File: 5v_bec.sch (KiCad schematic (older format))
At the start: 9 parts

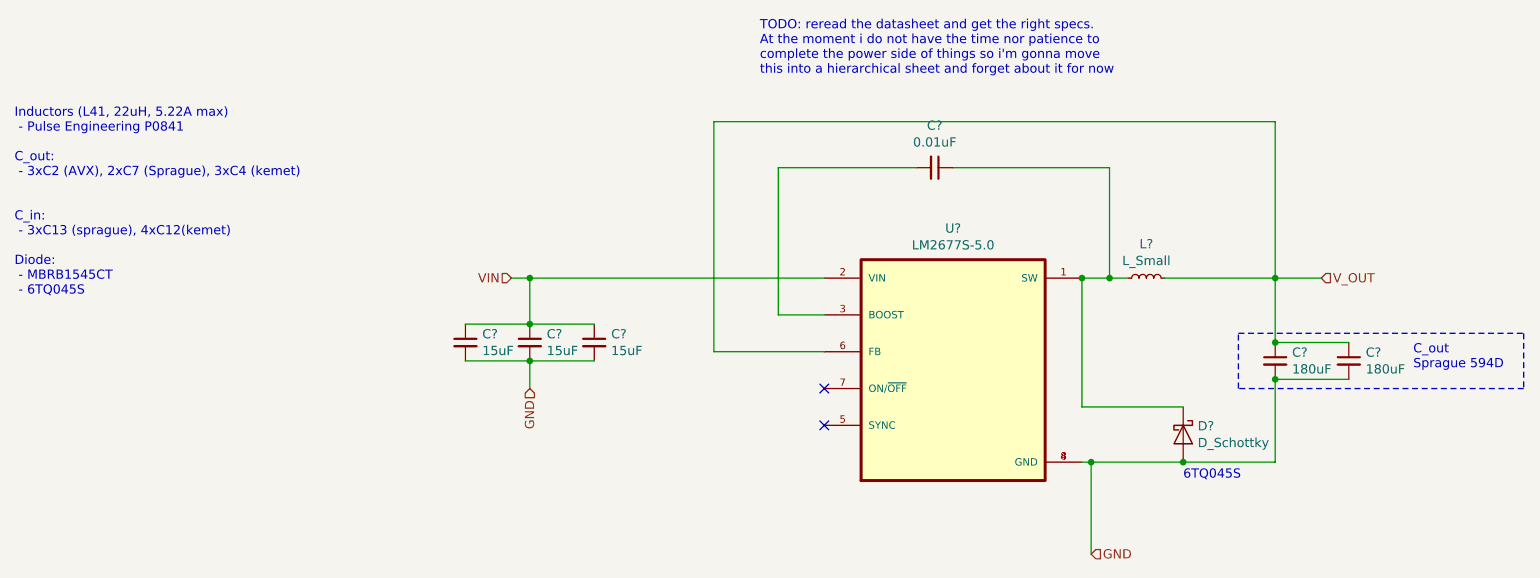
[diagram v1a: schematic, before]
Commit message: update reference ids, assign value to c8
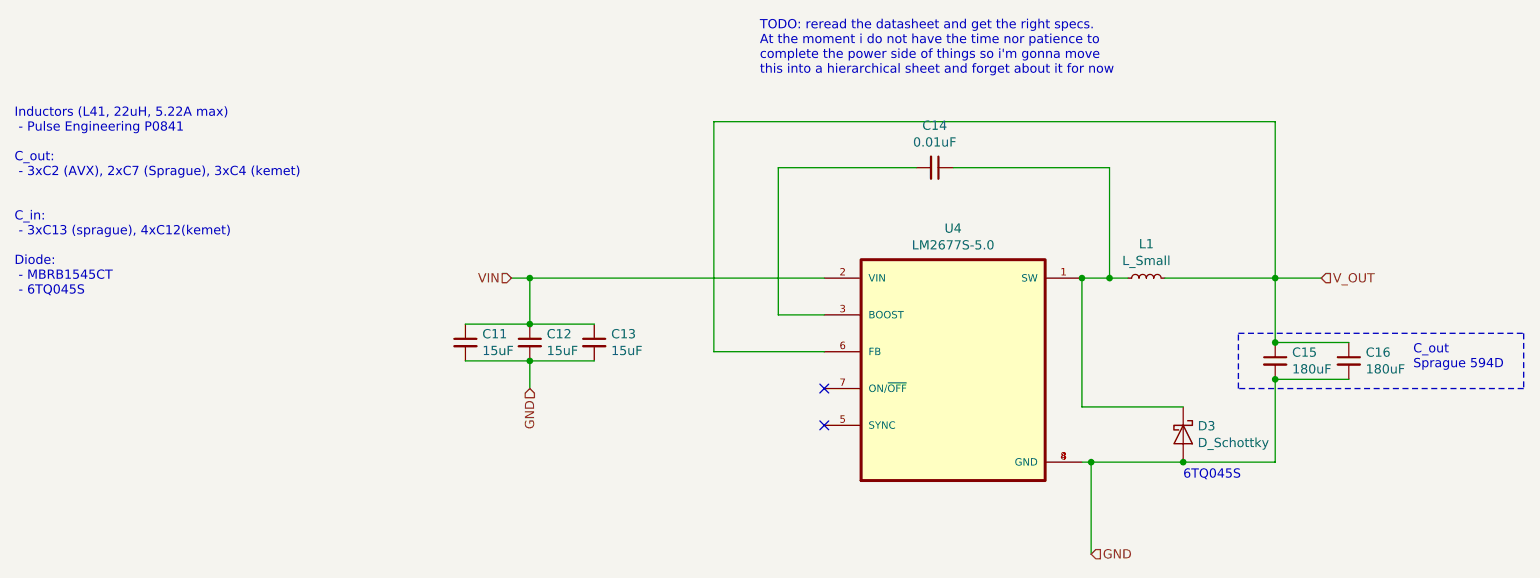
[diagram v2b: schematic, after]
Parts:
- gave numbers to parts that had none: 9
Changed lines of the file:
@@
 $Descr A4 11693 8268
 encoding utf-8
-Sheet 7 8
+Sheet 4 8
 Title ""
 Date ""
@@
 $EndDescr
 $Comp
-L LM2677S-5.0:LM2677S-5.0 U?
+L LM2677S-5.0:LM2677S-5.0 U4
 U 1 1 6175201D
 P 6000 4250
-AR Path="/6175047F/6175201D" Ref="U?"  Part="1"
+AR Path="/6175047F/6175201D" Ref="U4"  Part="1"
 AR Path="/617748F9/6175201D" Ref="U?"  Part="1"
 AR Path="/619B79F1/6175201D" Ref="U?"  Part="1"
-AR Path="/619C4F1E/6175201D" Ref="U?"  Part="1"
+AR Path="/619C4F1E/6175201D" Ref="U7"  Part="1"
 AR Path="/619C86ED/6175201D" Ref="U?"  Part="1"
-F 0 "U?" H 6000 5020 50  0000 C CNN
+F 0 "U4" H 6000 5020 50  0000 C CNN
 F 1 "LM2677S-5.0" H 6000 4929 50  0000 C CNN
 F 2 "TO127P1435X464-8N" H 6000 4250 50  0001 L BNN
@@
 	6750 4750 6700 4750
 $Comp
-L Device:D_Schottky D?
+L Device:D_Schottky D3
 U 1 1 617603E2
 P 7250 4600
-AR Path="/6175047F/617603E2" Ref="D?"  Part="1"
+AR Path="/6175047F/617603E2" Ref="D3"  Part="1"
 AR Path="/617748F9/617603E2" Ref="D?"  Part="1"
 AR Path="/619B79F1/617603E2" Ref="D?"  Part="1"
-AR Path="/619C4F1E/617603E2" Ref="D?"  Part="1"
+AR Path="/619C4F1E/617603E2" Ref="D6"  Part="1"
 AR Path="/619C86ED/617603E2" Ref="D?"  Part="1"
-F 0 "D?" V 7204 4679 50  0000 L CNN
+F 0 "D3" V 7204 4679 50  0000 L CNN
 F 1 "D_Schottky" V 7295 4679 50  0000 L CNN
 F 2 "" H 7250 4600 50  0001 C CNN
@@
 	6750 4750 7250 4750
 $Comp
-L Device:L_Small L?
+L Device:L_Small L1
 U 1 1 61768ED3
 P 7050 3750
-AR Path="/6175047F/61768ED3" Ref="L?"  Part="1"
+AR Path="/6175047F/61768ED3" Ref="L1"  Part="1"
 AR Path="/617748F9/61768ED3" Ref="L?"  Part="1"
 AR Path="/619B79F1/61768ED3" Ref="L?"  Part="1"
-AR Path="/619C4F1E/61768ED3" Ref="L?"  Part="1"
+AR Path="/619C4F1E/61768ED3" Ref="L2"  Part="1"
 AR Path="/619C86ED/61768ED3" Ref="L?"  Part="1"
-F 0 "L?" V 7235 3750 50  0000 C CNN
+F 0 "L1" V 7235 3750 50  0000 C CNN
 F 1 "L_Small" V 7144 3750 50  0000 C CNN
 F 2 "" H 7050 3750 50  0001 C CNN
@@
 	6850 3750 6950 3750
 $Comp
-L Device:C_Small C?
+L Device:C_Small C14
 U 1 1 6176CADF
 P 5900 3150
-AR Path="/6175047F/6176CADF" Ref="C?"  Part="1"
+AR Path="/6175047F/6176CADF" Ref="C14"  Part="1"
 AR Path="/617748F9/6176CADF" Ref="C?"  Part="1"
 AR Path="/619B79F1/6176CADF" Ref="C?"  Part="1"
-AR Path="/619C4F1E/6176CADF" Ref="C?"  Part="1"
+AR Path="/619C4F1E/6176CADF" Ref="C25"  Part="1"
 AR Path="/619C86ED/6176CADF" Ref="C?"  Part="1"
-F 0 "C?" V 5671 3150 50  0000 C CNN
+F 0 "C14" V 5671 3150 50  0000 C CNN
 F 1 "0.01uF" V 5762 3150 50  0000 C CNN
 F 2 "" H 5900 3150 50  0001 C CNN
@@
 Inductors (L41, 22uH, 5.22A max)\n - Pulse Engineering P0841\n\nC_out:\n - 3xC2 (AVX), 2xC7 (Sprague), 3xC4 (kemet)\n\n\nC_in:\n - 3xC13 (sprague), 4xC12(kemet)\n\nDiode: \n - MBRB1545CT\n - 6TQ045S
 $Comp
-L Device:C_Small C?
+L Device:C_Small C15
 U 1 1 61A51E59
 P 7750 4200
-AR Path="/6175047F/61A51E59" Ref="C?"  Part="1"
-AR Path="/619C4F1E/61A51E59" Ref="C?"  Part="1"
-F 0 "C?" H 7842 4246 50  0000 L CNN
+AR Path="/6175047F/61A51E59" Ref="C15"  Part="1"
+AR Path="/619C4F1E/61A51E59" Ref="C26"  Part="1"
+F 0 "C15" H 7842 4246 50  0000 L CNN
 F 1 "180uF" H 7842 4155 50  0000 L CNN
 F 2 "" H 7750 4200 50  0001 C CNN
@@
 $EndComp
 $Comp
-L Device:C_Small C?
+L Device:C_Small C16
 U 1 1 61A52F3A
 P 8150 4200
-AR Path="/6175047F/61A52F3A" Ref="C?"  Part="1"
-AR Path="/619C4F1E/61A52F3A" Ref="C?"  Part="1"
-F 0 "C?" H 8242 4246 50  0000 L CNN
+AR Path="/6175047F/61A52F3A" Ref="C16"  Part="1"
+AR Path="/619C4F1E/61A52F3A" Ref="C27"  Part="1"
+F 0 "C16" H 8242 4246 50  0000 L CNN
 F 1 "180uF" H 8242 4155 50  0000 L CNN
 F 2 "" H 8150 4200 50  0001 C CNN
@@
 	3600 3750 3700 3750
 $Comp
-L Device:C_Small C?
+L Device:C_Small C11
 U 1 1 61A5F9C8
 P 3350 4100
-AR Path="/6175047F/61A5F9C8" Ref="C?"  Part="1"
-AR Path="/619C4F1E/61A5F9C8" Ref="C?"  Part="1"
-F 0 "C?" H 3442 4146 50  0000 L CNN
+AR Path="/6175047F/61A5F9C8" Ref="C11"  Part="1"
+AR Path="/619C4F1E/61A5F9C8" Ref="C22"  Part="1"
+F 0 "C11" H 3442 4146 50  0000 L CNN
 F 1 "15uF" H 3442 4055 50  0000 L CNN
 F 2 "" H 3350 4100 50  0001 C CNN
@@
 $EndComp
 $Comp
-L Device:C_Small C?
+L Device:C_Small C12
 U 1 1 61A60CAD
 P 3700 4100
-AR Path="/6175047F/61A60CAD" Ref="C?"  Part="1"
-AR Path="/619C4F1E/61A60CAD" Ref="C?"  Part="1"
-F 0 "C?" H 3792 4146 50  0000 L CNN
+AR Path="/6175047F/61A60CAD" Ref="C12"  Part="1"
+AR Path="/619C4F1E/61A60CAD" Ref="C23"  Part="1"
+F 0 "C12" H 3792 4146 50  0000 L CNN
 F 1 "15uF" H 3792 4055 50  0000 L CNN
 F 2 "" H 3700 4100 50  0001 C CNN
@@
 $EndComp
 $Comp
-L Device:C_Small C?
+L Device:C_Small C13
 U 1 1 61A62459
 P 4050 4100
-AR Path="/6175047F/61A62459" Ref="C?"  Part="1"
-AR Path="/619C4F1E/61A62459" Ref="C?"  Part="1"
-F 0 "C?" H 4142 4146 50  0000 L CNN
+AR Path="/6175047F/61A62459" Ref="C13"  Part="1"
+AR Path="/619C4F1E/61A62459" Ref="C24"  Part="1"
+F 0 "C13" H 4142 4146 50  0000 L CNN
 F 1 "15uF" H 4142 4055 50  0000 L CNN
 F 2 "" H 4050 4100 50  0001 C CNN

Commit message: no longer a hat lol
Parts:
- C11, C12, C13: footprint (none) -> Capacitor_Tantalum_SMD:CP_EIA-7260-15_AVX-R_Pad2.68x6.30mm_HandSolder
- C14: footprint (none) -> Capacitor_SMD:C_0805_2012Metric_Pad1.15x1.40mm_HandSolder
- C15, C16: footprint (none) -> Capacitor_Tantalum_SMD:CP_EIA-7260-38_AVX-R_Pad2.68x6.30mm_HandSolder
- D3: footprint (none) -> TO254P1521X483-4N:TO254P1521X483-4N
- L1: value L_Small -> 22uH; footprint (none) -> Inductor_SMD:L_10.4x10.4_H4.8
- U4: footprint TO127P1435X464-8N -> LM2677S-5:TO127P1435X464-8N
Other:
- note added: "C_in\nSprague 594D"
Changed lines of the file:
@@
 $Descr A4 11693 8268
 encoding utf-8
-Sheet 4 8
+Sheet 7 8
 Title ""
 Date ""
@@
 AR Path="/619C4F1E/6175201D" Ref="U7"  Part="1"
 AR Path="/619C86ED/6175201D" Ref="U?"  Part="1"
-F 0 "U4" H 6000 5020 50  0000 C CNN
+F 0 "U7" H 6000 5020 50  0000 C CNN
 F 1 "LM2677S-5.0" H 6000 4929 50  0000 C CNN
-F 2 "TO127P1435X464-8N" H 6000 4250 50  0001 L BNN
+F 2 "LM2677S-5:TO127P1435X464-8N" H 6000 4250 50  0001 L BNN
 F 3 "" H 6000 4250 50  0001 L BNN
 	1    6000 4250
@@
 AR Path="/619C4F1E/617603E2" Ref="D6"  Part="1"
 AR Path="/619C86ED/617603E2" Ref="D?"  Part="1"
-F 0 "D3" V 7204 4679 50  0000 L CNN
+F 0 "D6" V 7204 4679 50  0000 L CNN
 F 1 "D_Schottky" V 7295 4679 50  0000 L CNN
-F 2 "" H 7250 4600 50  0001 C CNN
+F 2 "TO254P1521X483-4N:TO254P1521X483-4N" H 7250 4600 50  0001 C CNN
 F 3 "~" H 7250 4600 50  0001 C CNN
 	1    7250 4600
@@
 AR Path="/619C4F1E/61768ED3" Ref="L2"  Part="1"
 AR Path="/619C86ED/61768ED3" Ref="L?"  Part="1"
-F 0 "L1" V 7235 3750 50  0000 C CNN
-F 1 "L_Small" V 7144 3750 50  0000 C CNN
-F 2 "" H 7050 3750 50  0001 C CNN
+F 0 "L2" V 7235 3750 50  0000 C CNN
+F 1 "22uH" V 7144 3750 50  0000 C CNN
+F 2 "Inductor_SMD:L_10.4x10.4_H4.8" H 7050 3750 50  0001 C CNN
 F 3 "~" H 7050 3750 50  0001 C CNN
 	1    7050 3750
@@
 AR Path="/619C4F1E/6176CADF" Ref="C25"  Part="1"
 AR Path="/619C86ED/6176CADF" Ref="C?"  Part="1"
-F 0 "C14" V 5671 3150 50  0000 C CNN
+F 0 "C25" V 5671 3150 50  0000 C CNN
 F 1 "0.01uF" V 5762 3150 50  0000 C CNN
-F 2 "" H 5900 3150 50  0001 C CNN
+F 2 "Capacitor_SMD:C_0805_2012Metric_Pad1.15x1.40mm_HandSolder" H 5900 3150 50  0001 C CNN
 F 3 "~" H 5900 3150 50  0001 C CNN
 	1    5900 3150
@@
 AR Path="/6175047F/61A51E59" Ref="C15"  Part="1"
 AR Path="/619C4F1E/61A51E59" Ref="C26"  Part="1"
-F 0 "C15" H 7842 4246 50  0000 L CNN
+F 0 "C26" H 7842 4246 50  0000 L CNN
 F 1 "180uF" H 7842 4155 50  0000 L CNN
-F 2 "" H 7750 4200 50  0001 C CNN
+F 2 "Capacitor_Tantalum_SMD:CP_EIA-7260-38_AVX-R_Pad2.68x6.30mm_HandSolder" H 7750 4200 50  0001 C CNN
 F 3 "~" H 7750 4200 50  0001 C CNN
 	1    7750 4200
@@
 AR Path="/6175047F/61A52F3A" Ref="C16"  Part="1"
 AR Path="/619C4F1E/61A52F3A" Ref="C27"  Part="1"
-F 0 "C16" H 8242 4246 50  0000 L CNN
+F 0 "C27" H 8242 4246 50  0000 L CNN
 F 1 "180uF" H 8242 4155 50  0000 L CNN
-F 2 "" H 8150 4200 50  0001 C CNN
+F 2 "Capacitor_Tantalum_SMD:CP_EIA-7260-38_AVX-R_Pad2.68x6.30mm_HandSolder" H 8150 4200 50  0001 C CNN
 F 3 "~" H 8150 4200 50  0001 C CNN
 	1    8150 4200
@@
 AR Path="/6175047F/61A5F9C8" Ref="C11"  Part="1"
 AR Path="/619C4F1E/61A5F9C8" Ref="C22"  Part="1"
-F 0 "C11" H 3442 4146 50  0000 L CNN
+F 0 "C22" H 3442 4146 50  0000 L CNN
 F 1 "15uF" H 3442 4055 50  0000 L CNN
-F 2 "" H 3350 4100 50  0001 C CNN
+F 2 "Capacitor_Tantalum_SMD:CP_EIA-7260-15_AVX-R_Pad2.68x6.30mm_HandSolder" H 3350 4100 50  0001 C CNN
 F 3 "~" H 3350 4100 50  0001 C CNN
 	1    3350 4100
@@
 AR Path="/6175047F/61A60CAD" Ref="C12"  Part="1"
 AR Path="/619C4F1E/61A60CAD" Ref="C23"  Part="1"
-F 0 "C12" H 3792 4146 50  0000 L CNN
+F 0 "C23" H 3792 4146 50  0000 L CNN
 F 1 "15uF" H 3792 4055 50  0000 L CNN
-F 2 "" H 3700 4100 50  0001 C CNN
+F 2 "Capacitor_Tantalum_SMD:CP_EIA-7260-15_AVX-R_Pad2.68x6.30mm_HandSolder" H 3700 4100 50  0001 C CNN
 F 3 "~" H 3700 4100 50  0001 C CNN
 	1    3700 4100
@@
 AR Path="/6175047F/61A62459" Ref="C13"  Part="1"
 AR Path="/619C4F1E/61A62459" Ref="C24"  Part="1"
-F 0 "C13" H 4142 4146 50  0000 L CNN
+F 0 "C24" H 4142 4146 50  0000 L CNN
 F 1 "15uF" H 4142 4055 50  0000 L CNN
-F 2 "" H 4050 4100 50  0001 C CNN
+F 2 "Capacitor_Tantalum_SMD:CP_EIA-7260-15_AVX-R_Pad2.68x6.30mm_HandSolder" H 4050 4100 50  0001 C CNN
 F 3 "~" H 4050 4100 50  0001 C CNN
 	1    4050 4100
@@
 Text Notes 7250 4850 0    50   ~ 0
 6TQ045S
+Wire Notes Line
+	4400 4300 2700 4300
+Wire Notes Line
+	2700 4300 2700 3900
+Wire Notes Line
+	2700 3900 4400 3900
+Wire Notes Line
+	4400 3900 4400 4300
+Text Notes 2750 4250 0    50   ~ 0
+C_in\nSprague 594D
 $EndSCHEMATC

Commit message: power supply overhaul
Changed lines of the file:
@@
 $Descr A4 11693 8268
 encoding utf-8
-Sheet 7 8
+Sheet 7 10
 Title ""
 Date ""
@@
 AR Path="/619C4F1E/6175201D" Ref="U7"  Part="1"
 AR Path="/619C86ED/6175201D" Ref="U?"  Part="1"
-F 0 "U7" H 6000 5020 50  0000 C CNN
+F 0 "U4" H 6000 5020 50  0000 C CNN
 F 1 "LM2677S-5.0" H 6000 4929 50  0000 C CNN
 F 2 "LM2677S-5:TO127P1435X464-8N" H 6000 4250 50  0001 L BNN
@@
 AR Path="/619C4F1E/617603E2" Ref="D6"  Part="1"
 AR Path="/619C86ED/617603E2" Ref="D?"  Part="1"
-F 0 "D6" V 7204 4679 50  0000 L CNN
+F 0 "D3" V 7204 4679 50  0000 L CNN
 F 1 "D_Schottky" V 7295 4679 50  0000 L CNN
 F 2 "TO254P1521X483-4N:TO254P1521X483-4N" H 7250 4600 50  0001 C CNN
@@
 AR Path="/619C4F1E/61768ED3" Ref="L2"  Part="1"
 AR Path="/619C86ED/61768ED3" Ref="L?"  Part="1"
-F 0 "L2" V 7235 3750 50  0000 C CNN
+F 0 "L1" V 7235 3750 50  0000 C CNN
 F 1 "22uH" V 7144 3750 50  0000 C CNN
 F 2 "Inductor_SMD:L_10.4x10.4_H4.8" H 7050 3750 50  0001 C CNN
@@
 AR Path="/619C4F1E/6176CADF" Ref="C25"  Part="1"
 AR Path="/619C86ED/6176CADF" Ref="C?"  Part="1"
-F 0 "C25" V 5671 3150 50  0000 C CNN
+F 0 "C14" V 5671 3150 50  0000 C CNN
 F 1 "0.01uF" V 5762 3150 50  0000 C CNN
 F 2 "Capacitor_SMD:C_0805_2012Metric_Pad1.15x1.40mm_HandSolder" H 5900 3150 50  0001 C CNN
@@
 AR Path="/6175047F/61A51E59" Ref="C15"  Part="1"
 AR Path="/619C4F1E/61A51E59" Ref="C26"  Part="1"
-F 0 "C26" H 7842 4246 50  0000 L CNN
+F 0 "C15" H 7842 4246 50  0000 L CNN
 F 1 "180uF" H 7842 4155 50  0000 L CNN
 F 2 "Capacitor_Tantalum_SMD:CP_EIA-7260-38_AVX-R_Pad2.68x6.30mm_HandSolder" H 7750 4200 50  0001 C CNN
@@
 AR Path="/6175047F/61A52F3A" Ref="C16"  Part="1"
 AR Path="/619C4F1E/61A52F3A" Ref="C27"  Part="1"
-F 0 "C27" H 8242 4246 50  0000 L CNN
+F 0 "C16" H 8242 4246 50  0000 L CNN
 F 1 "180uF" H 8242 4155 50  0000 L CNN
 F 2 "Capacitor_Tantalum_SMD:CP_EIA-7260-38_AVX-R_Pad2.68x6.30mm_HandSolder" H 8150 4200 50  0001 C CNN
@@
 AR Path="/6175047F/61A5F9C8" Ref="C11"  Part="1"
 AR Path="/619C4F1E/61A5F9C8" Ref="C22"  Part="1"
-F 0 "C22" H 3442 4146 50  0000 L CNN
+F 0 "C11" H 3442 4146 50  0000 L CNN
 F 1 "15uF" H 3442 4055 50  0000 L CNN
 F 2 "Capacitor_Tantalum_SMD:CP_EIA-7260-15_AVX-R_Pad2.68x6.30mm_HandSolder" H 3350 4100 50  0001 C CNN
@@
 AR Path="/6175047F/61A60CAD" Ref="C12"  Part="1"
 AR Path="/619C4F1E/61A60CAD" Ref="C23"  Part="1"
-F 0 "C23" H 3792 4146 50  0000 L CNN
+F 0 "C12" H 3792 4146 50  0000 L CNN
 F 1 "15uF" H 3792 4055 50  0000 L CNN
 F 2 "Capacitor_Tantalum_SMD:CP_EIA-7260-15_AVX-R_Pad2.68x6.30mm_HandSolder" H 3700 4100 50  0001 C CNN
@@
 AR Path="/6175047F/61A62459" Ref="C13"  Part="1"
 AR Path="/619C4F1E/61A62459" Ref="C24"  Part="1"
-F 0 "C24" H 4142 4146 50  0000 L CNN
+F 0 "C13" H 4142 4146 50  0000 L CNN
 F 1 "15uF" H 4142 4055 50  0000 L CNN
 F 2 "Capacitor_Tantalum_SMD:CP_EIA-7260-15_AVX-R_Pad2.68x6.30mm_HandSolder" H 4050 4100 50  0001 C CNN
